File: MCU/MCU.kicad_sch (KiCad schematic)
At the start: 47 parts, among them J101 Power_Conn, J102 MCU_UART_Conn, J103 MCU_CAM_UART_Conn, J104 920MHz_Conn, J105 I2C_Conn, J106 I2C_Conn, J107 Motor_Conn, J108 CdS_Conn, J109 Power_EN_Conn, J110 I2C_Conn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

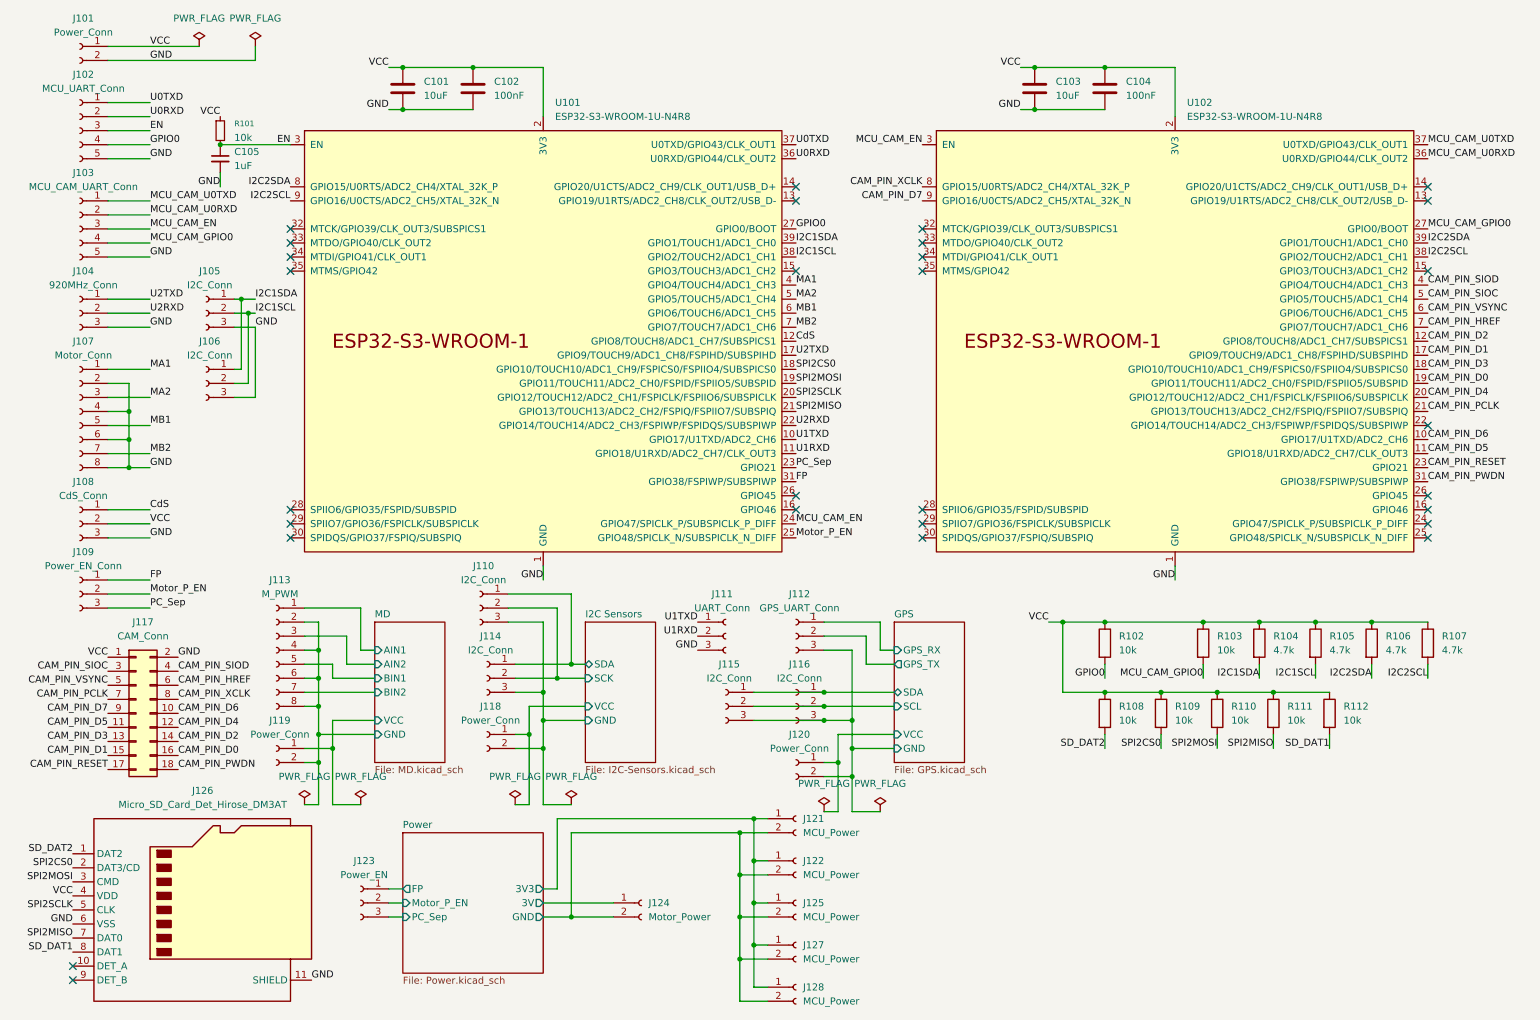
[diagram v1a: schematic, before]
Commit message: Update: コネクタをだいぶ消した
手配線になるね
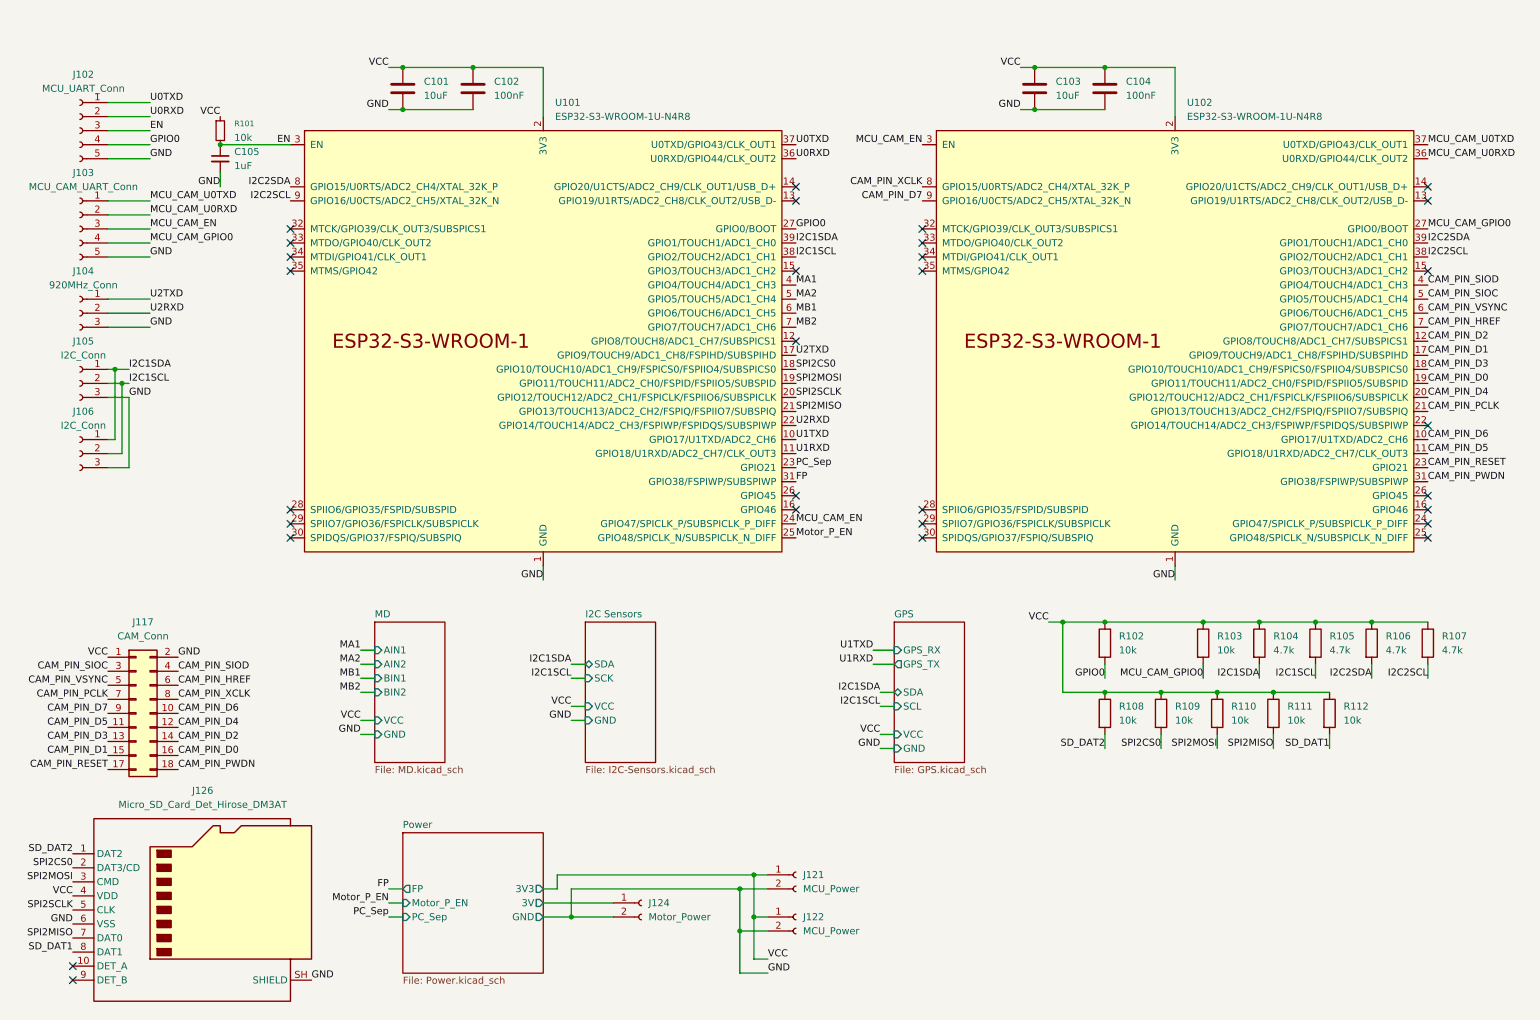
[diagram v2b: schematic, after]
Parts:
- removed J101, J118, J119, J120: Power_Conn, Connector_JST:JST_XH_B2B-XH-A_1x02_P2.50mm_Vertical, symbol Connector:Conn_01x02_Socket
- removed J107: Motor_Conn, Connector_JST:JST_XH_B8B-XH-A_1x08_P2.50mm_Vertical, symbol Connector:Conn_01x08_Socket
- removed J108: CdS_Conn, Connector_JST:JST_XH_B3B-XH-A_1x03_P2.50mm_Vertical, symbol Connector:Conn_01x03_Socket
- removed J109: Power_EN_Conn, Connector_JST:JST_XH_B3B-XH-A_1x03_P2.50mm_Vertical, symbol Connector:Conn_01x03_Socket
- removed J110, J114, J115, J116: I2C_Conn, Connector_JST:JST_XH_B3B-XH-A_1x03_P2.50mm_Vertical, symbol Connector:Conn_01x03_Socket
- removed J111: UART_Conn, Connector_JST:JST_XH_B3B-XH-A_1x03_P2.50mm_Vertical, symbol Connector:Conn_01x03_Socket
- removed J112: GPS_UART_Conn, Connector_JST:JST_XH_B3B-XH-A_1x03_P2.50mm_Vertical, symbol Connector:Conn_01x03_Socket
- removed J113: M_PWM, Connector_JST:JST_XH_B8B-XH-A_1x08_P2.50mm_Vertical, symbol Connector:Conn_01x08_Socket
- removed J123: Power_EN, Connector_JST:JST_XH_B3B-XH-A_1x03_P2.50mm_Vertical, symbol Connector:Conn_01x03_Socket
- removed J125, J127, J128: MCU_Power, Connector_JST:JST_XH_B2B-XH-A_1x02_P2.50mm_Vertical, symbol Connector:Conn_01x02_Socket
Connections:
- net Power/3V3 is gone; now on net VCC: J121.1 (Pin_1), J122.1 (Pin_1)
- net Power/GND is gone; now on net GND: J121.2 (Pin_2), J122.2 (Pin_2), J124.2 (Pin_2)
- net GND: now also J126.SH (SHIELD); no longer J126.11 (SHIELD)
- net CdS: no longer names the net of U101.12 (GPIO8/TOUCH8/ADC1_CH7/SUBSPICS1)
- no-connect marks 29 -> 30
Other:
- moved on the sheet: J105, J106, J121, J122
